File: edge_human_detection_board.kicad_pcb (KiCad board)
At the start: 4 copper layers, 4 parts, among them IC1 TXB0108PWR

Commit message: working on board
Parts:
- added C1: 0.1uF, Capacitor_SMD:C_0504_1310Metric_Pad0.83x1.28mm_HandSolder, F.Cu at (130.0, 87.0)
- added C2: 0.1uF, Capacitor_SMD:C_0504_1310Metric_Pad0.83x1.28mm_HandSolder, F.Cu at (118.0, 91.0)
- added C3: 0.1uF, Capacitor_SMD:C_0504_1310Metric_Pad0.83x1.28mm_HandSolder, F.Cu at (117.9, 99.0)
- added C4: 0.1uF, Capacitor_SMD:C_0504_1310Metric_Pad0.83x1.28mm_HandSolder, F.Cu at (118.0, 107.5)
- added D4: WS2812B, LED_SMD:LED_WS2812B_PLCC4_5.0x5.0mm_P3.2mm, F.Cu at (124.5, 109.0)
- added J1: Conn_01x03_Socket, Connector_PinHeader_2.54mm:PinHeader_1x03_P2.54mm_Vertical, F.Cu at (122.0, 54.0)
- added R1: 1.5k, Resistor_SMD:R_0805_2012Metric_Pad1.20x1.40mm_HandSolder, F.Cu at (126.5, 69.5)
- added REF**: MountingHole_2.2mm_M2, MountingHole:MountingHole_2.2mm_M2, F.Cu at (142.0, 117.5)
- added REF**: MountingHole_3.2mm_M3, MountingHole:MountingHole_3.2mm_M3, F.Cu at (168.5, 116.5)
- added REF**: MountingHole_3.2mm_M3, MountingHole:MountingHole_3.2mm_M3, F.Cu at (119.0, 116.5)
- added REF**: MountingHole_2.2mm_M2, MountingHole:MountingHole_2.2mm_M2, F.Cu at (154.0, 117.5)
- added REF**: MountingHole_3.2mm_M3, MountingHole:MountingHole_3.2mm_M3, F.Cu at (118.5, 37.0)
- added REF**: MountingHole_3.2mm_M3, MountingHole:MountingHole_3.2mm_M3, F.Cu at (168.0, 37.0)
- added U1: ~, 00_parts_lib:coral_micro_board_mating, F.Cu at (149.9, 79.2)
- added U2: ~, 00_parts_lib:SATEL-VL53L8A, F.Cu at (148.0, 41.2)
- D1: value WS2812B -> LED; footprint LED_SMD:LED_WS2812B_PLCC4_5.0x5.0mm_P3.2mm -> LED_SMD:LED_0805_2012Metric_Pad1.15x1.40mm_HandSolder
- moved IC1 36.8 mm to (122.0, 80.5)
- moved D3 23.6 mm to (124.5, 100.5)
- moved D2 22.8 mm to (124.5, 92.5)
- moved D1 22.3 mm to (121.0, 69.5)
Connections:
- D1 pad 1: /Coral Micro Breakouts/+5VDC -> GND
- D1 pad 2: Net-(D1-DOUT) -> Net-(D1-A)
- D2 pad 4: Net-(D1-DOUT) -> Net-(D2-DIN)
- D3 pad 2: unconnected-(D3-DOUT-Pad2) -> Net-(D3-DOUT)
- IC1 pad 20: Net-(D1-DIN) -> Net-(D2-DIN)
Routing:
- net /Coral Micro Breakouts/+5VDC: track 0.00 -> 68.4 mm
- net /Coral Micro Breakouts/SDA: track 0.00 -> 58.7 mm
- net /Coral Micro Breakouts/+1.8VDC_RGB: track 0.00 -> 57.8 mm, vias 0 -> 2
- net /Coral Micro Breakouts/+1.8VDC_TOF: track 0.00 -> 54.6 mm, vias 0 -> 2
- net /Coral Micro Breakouts/SCL: track 0.00 -> 51.1 mm
- net /Coral Micro Breakouts/PWM_1: track 0.00 -> 45.8 mm
- net /Coral Micro Breakouts/+3.3VDC: track 0.00 -> 40.6 mm
- net GND: track 0.00 -> 39.9 mm, vias 0 -> 11
- net /Coral Micro Breakouts/PWM_0: track 0.00 -> 26.8 mm, vias 0 -> 2
- net Net-(D2-DIN): track 0.00 -> 22.8 mm, vias 0 -> 2
- net /Coral Micro Breakouts/DEBUG_TX: track 0.00 -> 18.7 mm
- net /Coral Micro Breakouts/DEBUG_RX: track 0.00 -> 17.7 mm
- net Net-(D3-DOUT): track 0.00 -> 10.3 mm
- net Net-(D2-DOUT): track 0.00 -> 8.75 mm
- net Net-(D1-A): track 0.00 -> 3.47 mm
- added copper zone on In1.Cu, net GND
- added copper zone on In2.Cu, net GND
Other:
- board outline added: 58 x 87.5 mm
- board text added: "EDGE DETECTION BOARD REV 1.0.0 BY JC"

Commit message: made board
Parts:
- added G***: LOGO, LOGO, F.Cu at (128.0, 41.0)
- added R1: 0, Resistor_SMD:R_0805_2012Metric_Pad1.20x1.40mm_HandSolder, F.Cu at (129.0, 78.5)
- added R3: 0, Resistor_SMD:R_0805_2012Metric_Pad1.20x1.40mm_HandSolder, F.Cu at (128.5, 55.5)
- added R4: 0, Resistor_SMD:R_0805_2012Metric_Pad1.20x1.40mm_HandSolder, F.Cu at (166.5, 59.0)
- added R5: 0, Resistor_SMD:R_0805_2012Metric_Pad1.20x1.40mm_HandSolder, F.Cu at (169.5, 54.5)
- added TP1(PWM_0): TestPoint, TestPoint:TestPoint_Pad_D2.0mm, B.Cu at (126.5, 73.0)
- added TP10(GND): TestPoint, TestPoint:TestPoint_Pad_D2.0mm, B.Cu at (154.0, 66.5)
- added TP11(SDA): TestPoint, TestPoint:TestPoint_Pad_D2.0mm, B.Cu at (147.5, 82.0)
- added TP12(GND): TestPoint, TestPoint:TestPoint_Pad_D2.0mm, B.Cu at (142.0, 60.0)
- added TP13(PWM_1): TestPoint, TestPoint:TestPoint_Pad_D2.0mm, B.Cu at (142.0, 65.0)
- added TP14(GND): TestPoint, TestPoint:TestPoint_Pad_D2.0mm, B.Cu at (147.5, 86.5)
- added TP2(GND): TestPoint, TestPoint:TestPoint_Pad_D2.0mm, B.Cu at (120.5, 73.0)
- added TP3(SIG_RGB1): TestPoint, TestPoint:TestPoint_Pad_D2.0mm, B.Cu at (124.5, 88.5)
- added TP4(GND): TestPoint, TestPoint:TestPoint_Pad_D2.0mm, B.Cu at (124.5, 92.5)
- added TP5(SIG_RGB2): TestPoint, TestPoint:TestPoint_Pad_D2.0mm, B.Cu at (130.0, 97.5)
- added TP6(GND): TestPoint, TestPoint:TestPoint_Pad_D2.0mm, B.Cu at (130.0, 101.5)
- added TP7(SIG_RGB3): TestPoint, TestPoint:TestPoint_Pad_D2.0mm, B.Cu at (130.5, 107.0)
- added TP8(GND): TestPoint, TestPoint:TestPoint_Pad_D2.0mm, B.Cu at (130.5, 111.0)
- added TP9(SCL): TestPoint, TestPoint:TestPoint_Pad_D2.0mm, B.Cu at (154.0, 71.5)
- renumbered R1 to R2
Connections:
- net /Coral Micro Breakouts/PWM_0 renamed /RGB Signalling/SIG_IN_PWM0
- net /Coral Micro Breakouts/PWM_1 renamed /TOF Sensor/PWM_1
- net /Coral Micro Breakouts/SCL renamed /TOF Sensor/SCL
- net /Coral Micro Breakouts/SDA renamed /TOF Sensor/SDA
- net Net-(D2-DIN) renamed /RGB Signalling/SIG_IN_RGB1
- net Net-(D2-DOUT) renamed /RGB Signalling/SIG_IN_RGB2
- net Net-(D3-DOUT) renamed /RGB Signalling/SIG_IN_RGB3
- C1 pad 2: /Coral Micro Breakouts/+5VDC -> Net-(U1-VSYS)
- R2 pad 1: /Coral Micro Breakouts/+5VDC -> Net-(U1-VSYS)
- U1 pad 14: /Coral Micro Breakouts/+1.8VDC_RGB -> Net-(R3-Pad2)
- U1 pad 2: /Coral Micro Breakouts/+1.8VDC_TOF -> Net-(R4-Pad1)
- U1 pad 24: /Coral Micro Breakouts/+5VDC -> Net-(U1-VSYS)
- U1 pad 3: /Coral Micro Breakouts/+3.3VDC -> Net-(U1-3.3V)
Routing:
- net Net-(U1-VSYS): track 0.00 -> 22.2 mm
- net /Coral Micro Breakouts/+5VDC: track 68.4 -> 49.7 mm
- net /Coral Micro Breakouts/+3.3VDC: track 40.6 -> 23.8 mm
- net GND: track 39.9 -> 24.7 mm, vias 11 -> 30
- net Net-(U1-3.3V): track 0.00 -> 14.8 mm
- net Net-(R3-Pad2): track 0.00 -> 8.14 mm
- net /Coral Micro Breakouts/+1.8VDC_TOF: track 54.6 -> 62.7 mm, vias 2 -> 3
- net /TOF Sensor/SCL: track 51.1 -> 56.6 mm, vias 0 -> 1
- net /RGB Signalling/SIG_IN_RGB2: track 8.75 -> 13.9 mm, vias 0 -> 1
- net Net-(R4-Pad1): track 0.00 -> 4.75 mm
- net /TOF Sensor/SDA: track 58.7 -> 63.4 mm, vias 0 -> 1
- net /TOF Sensor/PWM_1: track 45.8 -> 50.3 mm, vias 0 -> 1
- net /Coral Micro Breakouts/+1.8VDC_RGB: track 57.8 -> 53.5 mm
- net /RGB Signalling/SIG_IN_RGB3: track 10.3 -> 14.6 mm, vias 0 -> 1
- net /RGB Signalling/SIG_IN_RGB1: track 22.8 -> 25.0 mm
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- added copper zone on B.Cu, net GND
- added copper zone on F.Cu, net GND
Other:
- board text added: "+1.8VDC(RGB)"
- board text added: "+1.8VDC(TOF)"
- board text added: "+3.3VDC(TOF)"
- board text added: "+5VDC"

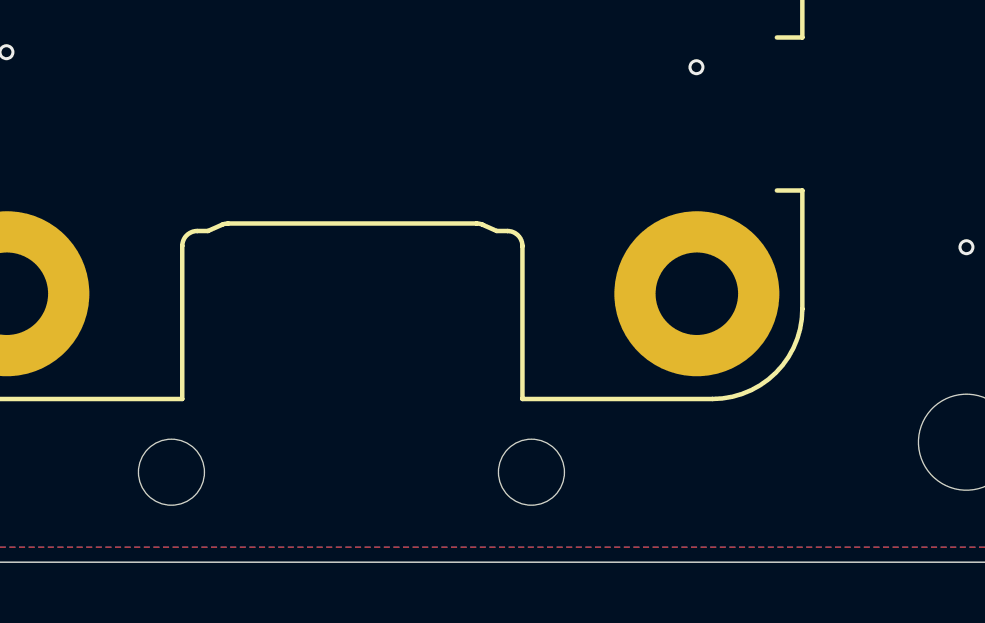
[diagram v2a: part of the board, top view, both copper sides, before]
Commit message: working on revisions
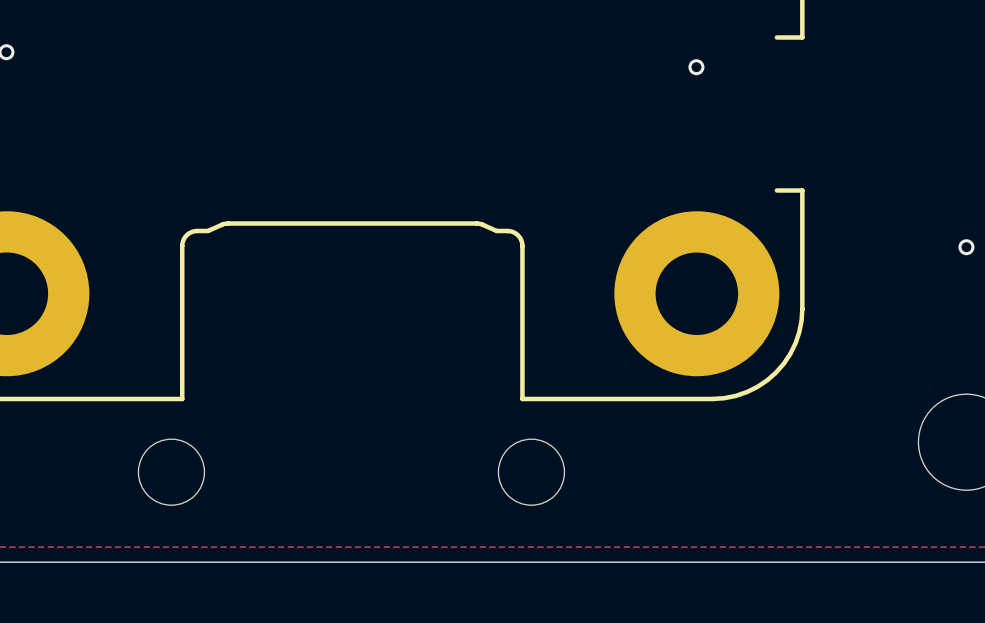
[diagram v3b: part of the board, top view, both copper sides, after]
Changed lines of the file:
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@@
 		(fp_arc
 			(start 30.77868 7.54868)
-			(mid 30.425147 7.402225)
+			(mid 30.425111 7.402231)
 			(end 30.27868 7.04868)
 			(stroke
@@
 		(fp_arc
 			(start 30.07185 6.22571)
-			(mid 30.039604 6.126355)
+			(mid 30.039591 6.126356)
 			(end 30.02868 6.02247)
 			(stroke
@@
 		(fp_arc
 			(start 30.02868 -2.26512)
-			(mid 30.039595 -2.369006)
+			(mid 30.039593 -2.369007)
 			(end 30.07185 -2.46836)
 			(stroke
@@
 		(fp_arc
 			(start 32.87868 -13.12132)
-			(mid 35.00002 -12.242649)
+			(mid 34.999985 -12.242643)
 			(end 35.87868 -10.12132)
 			(stroke

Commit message: latest
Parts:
- removed the REF** at (142.0, 117.5)
- removed the REF** at (168.5, 116.5)
- removed the REF** at (119.0, 116.5)
- removed the REF** at (154.0, 117.5)
- removed the REF** at (118.5, 37.0)
- removed the REF** at (168.0, 37.0)
- removed TP1(PWM_0), TP10(GND), TP11(SDA), TP12(GND), TP13(PWM_1), TP14(GND), TP2(GND), TP3(SIG_RGB1), TP4(GND), TP5(SIG_RGB2), TP6(GND), TP7(SIG_RGB3), TP8(GND), TP9(SCL): TestPoint, TestPoint:TestPoint_Pad_D2.0mm
- added C5: 100nF, Capacitor_SMD:C_0805_2012Metric_Pad1.18x1.45mm_HandSolder, F.Cu at (138.5, 38.5)
- added C6: 100nF, Capacitor_SMD:C_0805_2012Metric_Pad1.18x1.45mm_HandSolder, F.Cu at (147.5, 44.5)
- added C7: 47uF, Capacitor_SMD:C_0805_2012Metric_Pad1.18x1.45mm_HandSolder, F.Cu at (139.2, 34.6)
- added GND: TestPoint, TestPoint:TestPoint_Pad_D2.0mm, B.Cu at (153.2, 105.0)
- added GND: TestPoint, TestPoint:TestPoint_Pad_D2.0mm, B.Cu at (153.2, 80.0)
- added GND: TestPoint, TestPoint:TestPoint_Pad_D2.0mm, B.Cu at (153.2, 85.8)
- added GND: TestPoint, TestPoint:TestPoint_Pad_D2.0mm, B.Cu at (153.2, 111.0)
- added GND: TestPoint, TestPoint:TestPoint_Pad_D2.0mm, B.Cu at (153.2, 92.6)
- added GND: TestPoint, TestPoint:TestPoint_Pad_D2.0mm, B.Cu at (144.2, 67.6)
- added GND: TestPoint, TestPoint:TestPoint_Pad_D2.0mm, B.Cu at (153.2, 98.8)
- added LPN: TestPoint, TestPoint:TestPoint_Pad_D2.0mm, B.Cu at (144.2, 73.0)
- added PWM0: TestPoint, TestPoint:TestPoint_Pad_D2.0mm, B.Cu at (144.2, 92.2)
- added R10: 47k, Resistor_SMD:R_0805_2012Metric_Pad1.20x1.40mm_HandSolder, F.Cu at (160.5, 46.7)
- added R11: 47k, Resistor_SMD:R_0805_2012Metric_Pad1.20x1.40mm_HandSolder, F.Cu at (159.0, 40.0)
- added R12: 47k, Resistor_SMD:R_0805_2012Metric_Pad1.20x1.40mm_HandSolder, F.Cu at (159.0, 36.5)
- added R6: 2.2k, Resistor_SMD:R_0805_2012Metric_Pad1.20x1.40mm_HandSolder, F.Cu at (139.0, 46.7)
- added R7: 2.2k, Resistor_SMD:R_0805_2012Metric_Pad1.20x1.40mm_HandSolder, F.Cu at (143.5, 46.7)
- added R8: 47k, Resistor_SMD:R_0805_2012Metric_Pad1.20x1.40mm_HandSolder, F.Cu at (151.5, 46.7)
- added R9: 47k, Resistor_SMD:R_0805_2012Metric_Pad1.20x1.40mm_HandSolder, F.Cu at (156.0, 46.7)
- added REF**: MountingHole_3.2mm_M3, MountingHole:MountingHole_3.2mm_M3, F.Cu at (168.4, 37.4)
- added REF**: MountingHole_3.2mm_M3, MountingHole:MountingHole_3.2mm_M3, F.Cu at (119.2, 116.4)
- added REF**: MountingHole_3.2mm_M3, MountingHole:MountingHole_3.2mm_M3, F.Cu at (119.4, 38.0)
- added REF**: MountingHole_3.2mm_M3, MountingHole:MountingHole_3.2mm_M3, F.Cu at (168.2, 115.8)
- added REF**: MountingHole_2.2mm_M2, MountingHole:MountingHole_2.2mm_M2, F.Cu at (155.6, 117.0)
- added REF**: MountingHole_2.2mm_M2, MountingHole:MountingHole_2.2mm_M2, F.Cu at (141.4, 117.0)
- added RGB1: TestPoint, TestPoint:TestPoint_Pad_D2.0mm, B.Cu at (144.0, 98.8)
- added RGB2: TestPoint, TestPoint:TestPoint_Pad_D2.0mm, B.Cu at (144.0, 104.6)
- added RGB3: TestPoint, TestPoint:TestPoint_Pad_D2.0mm, B.Cu at (143.8, 110.8)
- added SCL: TestPoint, TestPoint:TestPoint_Pad_D2.0mm, B.Cu at (144.4, 85.4)
- added SDA: TestPoint, TestPoint:TestPoint_Pad_D2.0mm, B.Cu at (144.2, 79.6)
- D2, D3, D4: footprint LED_SMD:LED_WS2812B_PLCC4_5.0x5.0mm_P3.2mm -> 00_parts_lib:4684
- U2: footprint 00_parts_lib:SATEL-VL53L8A -> 00_parts_lib:VL53L8CXV0GC1
- moved U2 3.59 mm to (149.1, 37.8), turned to 90 degrees
- moved G*** 2.60 mm to (128.0, 43.6)
- turned D2 to -90 degrees
- turned D3 to -90 degrees
- turned D4 to -90 degrees
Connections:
- D2 pad 1: /Coral Micro Breakouts/+5VDC -> /RGB Signalling/SIG_IN_RGB2
- D2 pad 2: /RGB Signalling/SIG_IN_RGB2 -> GND
- D2 pad 3: GND -> /RGB Signalling/SIG_IN_RGB1
- D2 pad 4: /RGB Signalling/SIG_IN_RGB1 -> /Coral Micro Breakouts/+5VDC
- D3 pad 1: /Coral Micro Breakouts/+5VDC -> /RGB Signalling/SIG_IN_RGB3
- D3 pad 2: /RGB Signalling/SIG_IN_RGB3 -> GND
- D3 pad 3: GND -> /RGB Signalling/SIG_IN_RGB2
- D3 pad 4: /RGB Signalling/SIG_IN_RGB2 -> /Coral Micro Breakouts/+5VDC
- D4 pad 1: /Coral Micro Breakouts/+5VDC -> unconnected-(D4-DO-Pad1)
- D4 pad 2: unconnected-(D4-DOUT-Pad2) -> GND
- D4 pad 3: GND -> /RGB Signalling/SIG_IN_RGB3
- D4 pad 4: /RGB Signalling/SIG_IN_RGB3 -> /Coral Micro Breakouts/+5VDC
- R4 pad 2: /Coral Micro Breakouts/+1.8VDC_TOF -> /TOF Sensor/CORE_1V8
- R5 pad 2: /Coral Micro Breakouts/+3.3VDC -> /TOF Sensor/AVDD
- U1 pad 21: /TOF Sensor/PWM_1 -> /TOF Sensor/LPn
- U2 pad 1: GND -> Net-(U2-INT_1)
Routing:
- net /TOF Sensor/CORE_1V8: track 0.00 -> 97.2 mm, vias 0 -> 3
- net /TOF Sensor/AVDD: track 0.00 -> 70.9 mm, vias 0 -> 2
- net /Coral Micro Breakouts/+1.8VDC_TOF: track 62.7 -> 0.00 mm, vias 3 -> 0
- net /TOF Sensor/LPn: track 0.00 -> 58.1 mm, vias 0 -> 3
- net /TOF Sensor/PWM_1: track 50.3 -> 0.00 mm, vias 1 -> 0
- net /TOF Sensor/SCL: track 56.6 -> 82.6 mm
- net /Coral Micro Breakouts/+3.3VDC: track 23.8 -> 0.00 mm
- net /RGB Signalling/SIG_IN_RGB1: track 25.0 -> 41.5 mm
- net /RGB Signalling/SIG_IN_PWM0: track 28.9 -> 44.2 mm
- net /RGB Signalling/SIG_IN_RGB2: track 13.9 -> 28.7 mm
- net /RGB Signalling/SIG_IN_RGB3: track 14.6 -> 28.2 mm
- net Net-(U2-SYNC): track 0.00 -> 11.8 mm
- net /TOF Sensor/SDA: track 63.4 -> 74.0 mm, vias 1 -> 3
- net Net-(U2-NCS): track 0.00 -> 9.01 mm
- net Net-(U2-INT_1): track 0.00 -> 8.62 mm
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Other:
- board text added: "EDGE DETECTION BOARD REV 1.1.0 BY JC"
- board text added: "GND"
- board text added: "RX"
- board text added: "TX"
- board text removed: "+5VDC"
- board text removed: "EDGE DETECTION BOARD REV 1.0.0 BY JC"

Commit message: Fab v
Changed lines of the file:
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@@
 		(fp_arc
 			(start 30.77868 7.54868)
-			(mid 30.425147 7.402225)
+			(mid 30.425111 7.402231)
 			(end 30.27868 7.04868)
 			(stroke
@@
 		(fp_arc
 			(start 30.07185 6.22571)
-			(mid 30.039599 6.126356)
+			(mid 30.039598 6.126356)
 			(end 30.02868 6.02247)
 			(stroke
@@
 		(fp_arc
 			(start 30.02868 -2.26512)
-			(mid 30.039595 -2.369006)
+			(mid 30.039593 -2.369007)
 			(end 30.07185 -2.46836)
 			(stroke

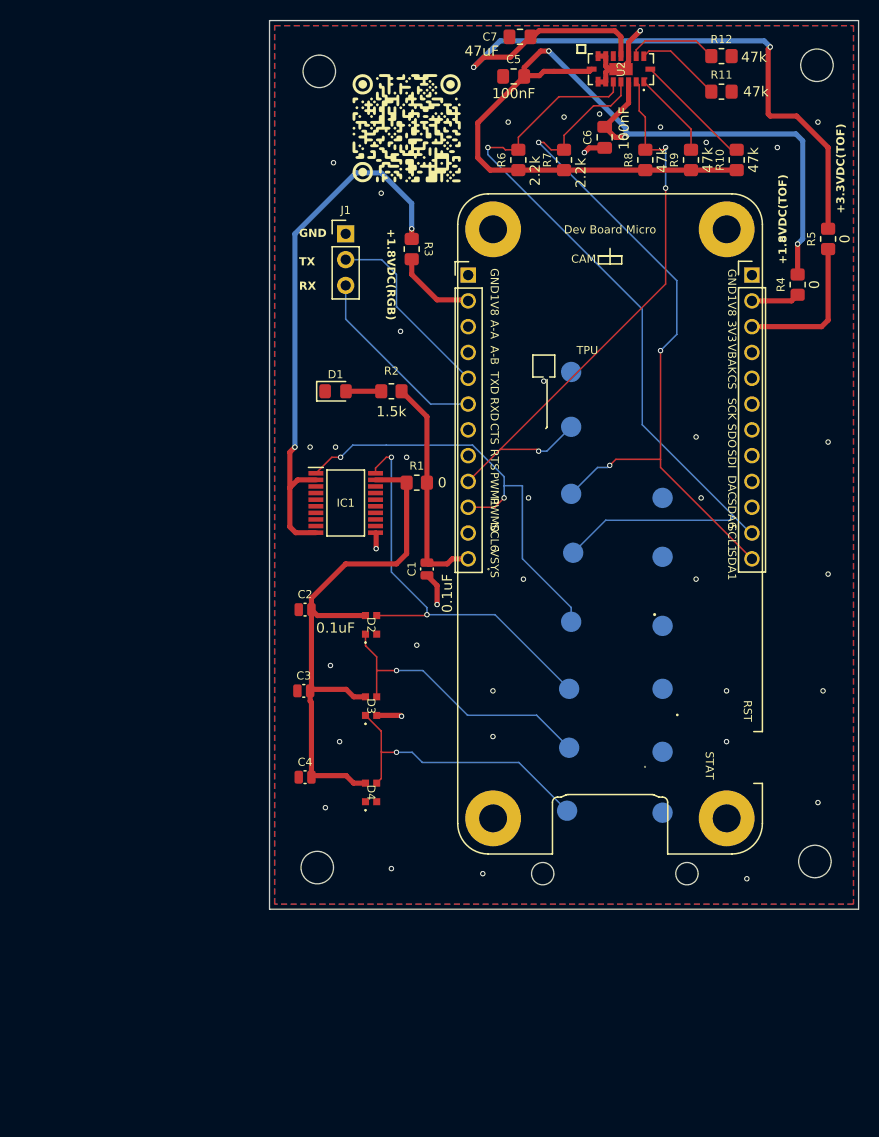
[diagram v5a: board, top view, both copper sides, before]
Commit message: not working, reverting to old design
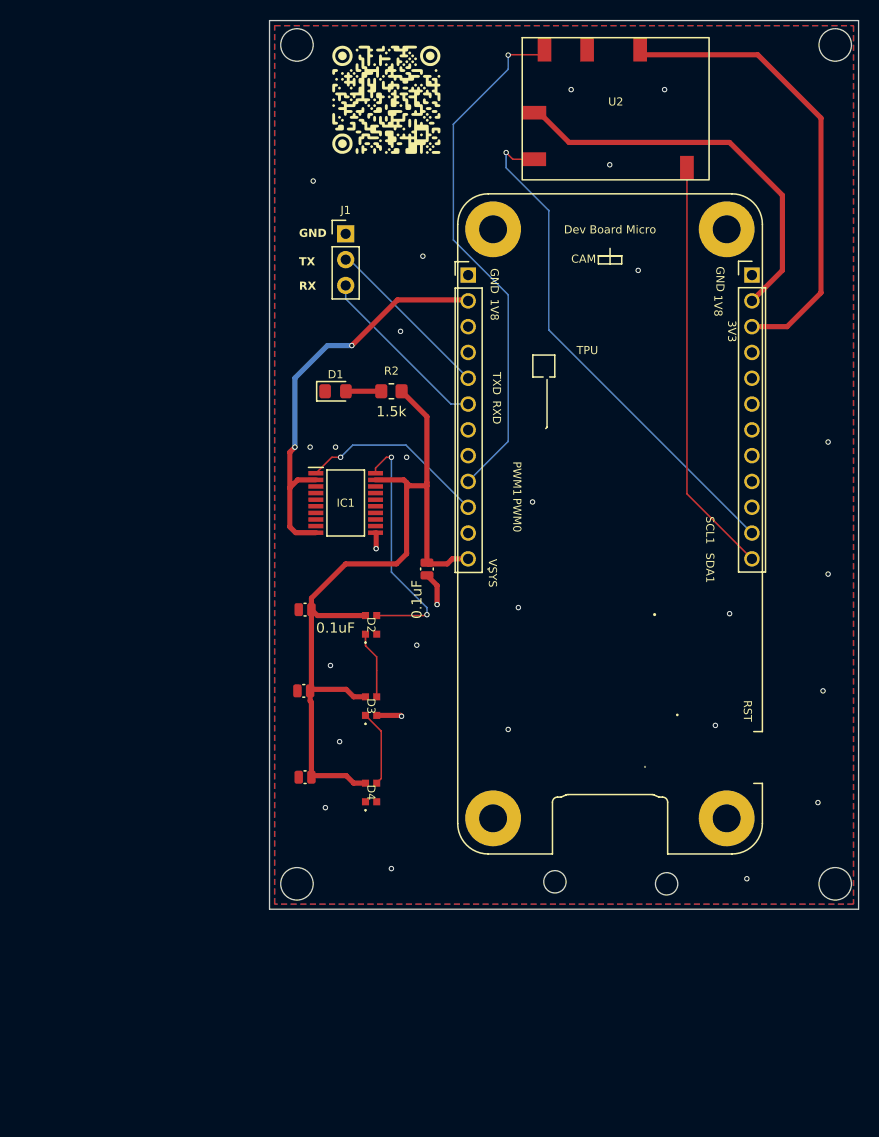
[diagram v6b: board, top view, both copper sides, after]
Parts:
- removed C5, C6: 100nF, Capacitor_SMD:C_0805_2012Metric_Pad1.18x1.45mm_HandSolder
- removed C7: 47uF, Capacitor_SMD:C_0805_2012Metric_Pad1.18x1.45mm_HandSolder
- removed GND (x7), LPN, PWM0, RGB1, RGB2, RGB3, SCL, SDA: TestPoint, TestPoint:TestPoint_Pad_D2.0mm
- removed R1, R3, R4, R5: 0, Resistor_SMD:R_0805_2012Metric_Pad1.20x1.40mm_HandSolder
- removed R10, R11, R12, R8, R9: 47k, Resistor_SMD:R_0805_2012Metric_Pad1.20x1.40mm_HandSolder
- removed R6, R7: 2.2k, Resistor_SMD:R_0805_2012Metric_Pad1.20x1.40mm_HandSolder
- removed the REF** at (168.4, 37.4)
- removed the REF** at (119.2, 116.4)
- removed the REF** at (119.4, 38.0)
- removed the REF** at (168.2, 115.8)
- removed the REF** at (155.6, 117.0)
- removed the REF** at (141.4, 117.0)
- added ?: , , F.Cu at (117.2, 35.4)
- added ?: , , F.Cu at (117.2, 118.0)
- added ?: , , F.Cu at (170.2, 35.4)
- added REF**: MountingHole_2.2mm_M2, MountingHole:MountingHole_2.2mm_M2, F.Cu at (142.6, 117.8)
- added REF**: MountingHole_2.2mm_M2, MountingHole:MountingHole_2.2mm_M2, F.Cu at (153.6, 118.0)
- added REF**: MountingHole_3.2mm_M3, MountingHole:MountingHole_3.2mm_M3, F.Cu at (170.2, 118.0)
- U2: footprint 00_parts_lib:VL53L8CXV0GC1 -> 00_parts_lib:TOF_MODULE
- moved U2 3.74 mm to (148.6, 41.5), turned to 0 degrees
- moved G*** 3.44 mm to (126.0, 40.8)
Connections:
- C1 pad 2: Net-(U1-VSYS) -> /Coral Micro Breakouts/+5VDC
- R2 pad 1: Net-(U1-VSYS) -> /Coral Micro Breakouts/+5VDC
- U1 pad 11: /TOF Sensor/SCL -> /Coral Micro Breakouts/SCL
- U1 pad 12: /TOF Sensor/SDA -> /Coral Micro Breakouts/SDA
- U1 pad 14: Net-(R3-Pad2) -> /Coral Micro Breakouts/+1.8VDC_RGB
- U1 pad 2: Net-(R4-Pad1) -> /Coral Micro Breakouts/+1.8VDC_TOF
- U1 pad 21: /TOF Sensor/LPn -> /Coral Micro Breakouts/PWM_1
- U1 pad 24: Net-(U1-VSYS) -> /Coral Micro Breakouts/+5VDC
- U1 pad 3: Net-(U1-3.3V) -> /Coral Micro Breakouts/+3.3VDC
- U2 pad 1: Net-(U2-INT_1) -> /Coral Micro Breakouts/SDA
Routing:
- net /TOF Sensor/CORE_1V8: track 97.2 -> 0.00 mm, vias 3 -> 0
- net /TOF Sensor/SCL: track 82.6 -> 0.00 mm, vias 1 -> 0
- net /TOF Sensor/SDA: track 74.0 -> 0.00 mm, vias 3 -> 0
- net /TOF Sensor/AVDD: track 70.9 -> 0.00 mm, vias 2 -> 0
- net /TOF Sensor/LPn: track 58.1 -> 0.00 mm, vias 3 -> 0
- net /Coral Micro Breakouts/PWM_1: track 0.00 -> 51.7 mm, vias 0 -> 1
- net /Coral Micro Breakouts/SCL: track 0.00 -> 51.2 mm, vias 0 -> 1
- net /Coral Micro Breakouts/+3.3VDC: track 0.00 -> 45.8 mm
- net /Coral Micro Breakouts/SDA: track 0.00 -> 41.7 mm
- net /Coral Micro Breakouts/+1.8VDC_TOF: track 0.00 -> 38.9 mm
- net /RGB Signalling/SIG_IN_PWM0: track 44.2 -> 18.7 mm, vias 2 -> 1
- net /Coral Micro Breakouts/+5VDC: track 56.2 -> 80.5 mm
- net Net-(U1-VSYS): track 22.2 -> 0.00 mm
- net /RGB Signalling/SIG_IN_RGB2: track 28.7 -> 6.63 mm, vias 1 -> 0
- net /RGB Signalling/SIG_IN_RGB3: track 28.2 -> 7.50 mm, vias 1 -> 0
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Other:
- board text removed: "+1.8VDC(RGB)"
- board text removed: "+1.8VDC(TOF)"
- board text removed: "+3.3VDC(TOF)"
